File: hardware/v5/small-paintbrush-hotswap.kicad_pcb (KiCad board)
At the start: 2 copper layers, 97 x 50 mm, 21 parts, among them J1 Conn_01x02, J2 Conn_01x04, J3 Conn_01x04, SW1 SW_SPDT, SW2 SW_SPDT, U1 ProMicro, U2 ProMicro

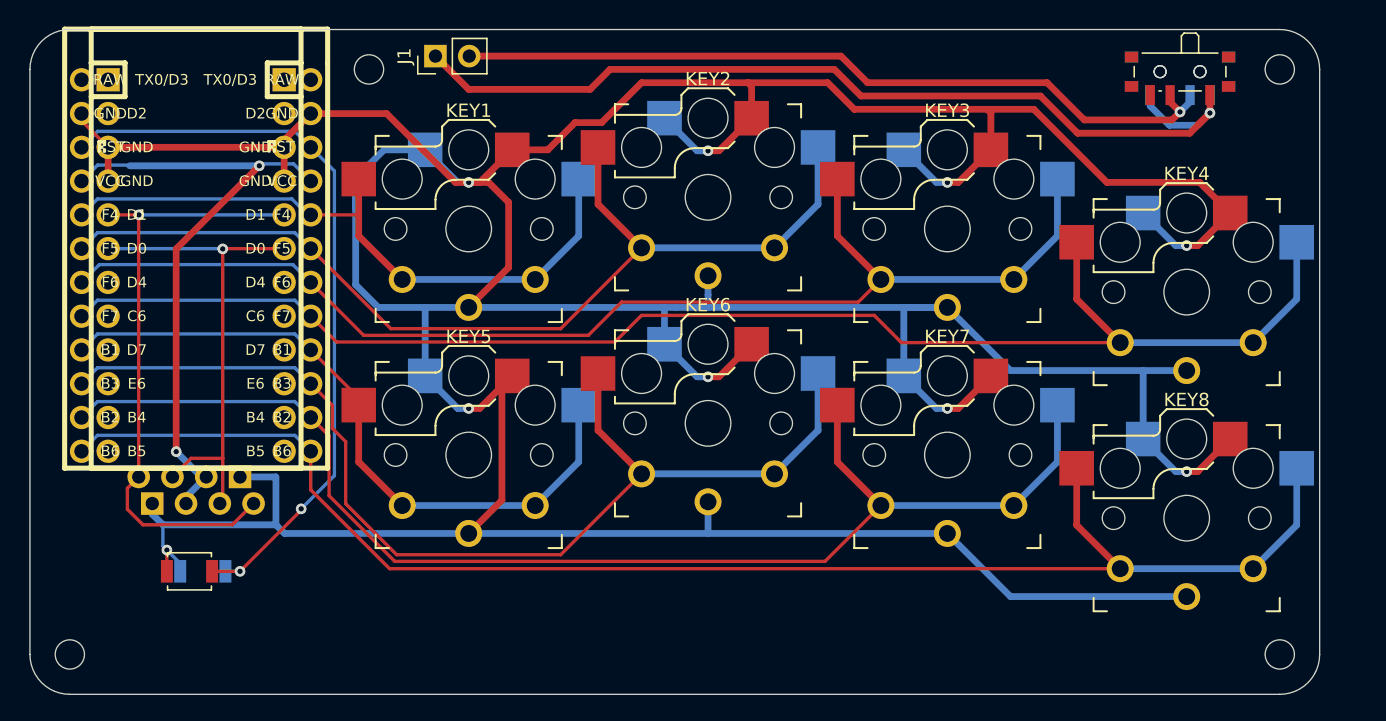
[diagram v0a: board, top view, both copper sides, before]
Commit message: v5 of the paintbrush with choc and mx hot swap switches (pcb size changed)
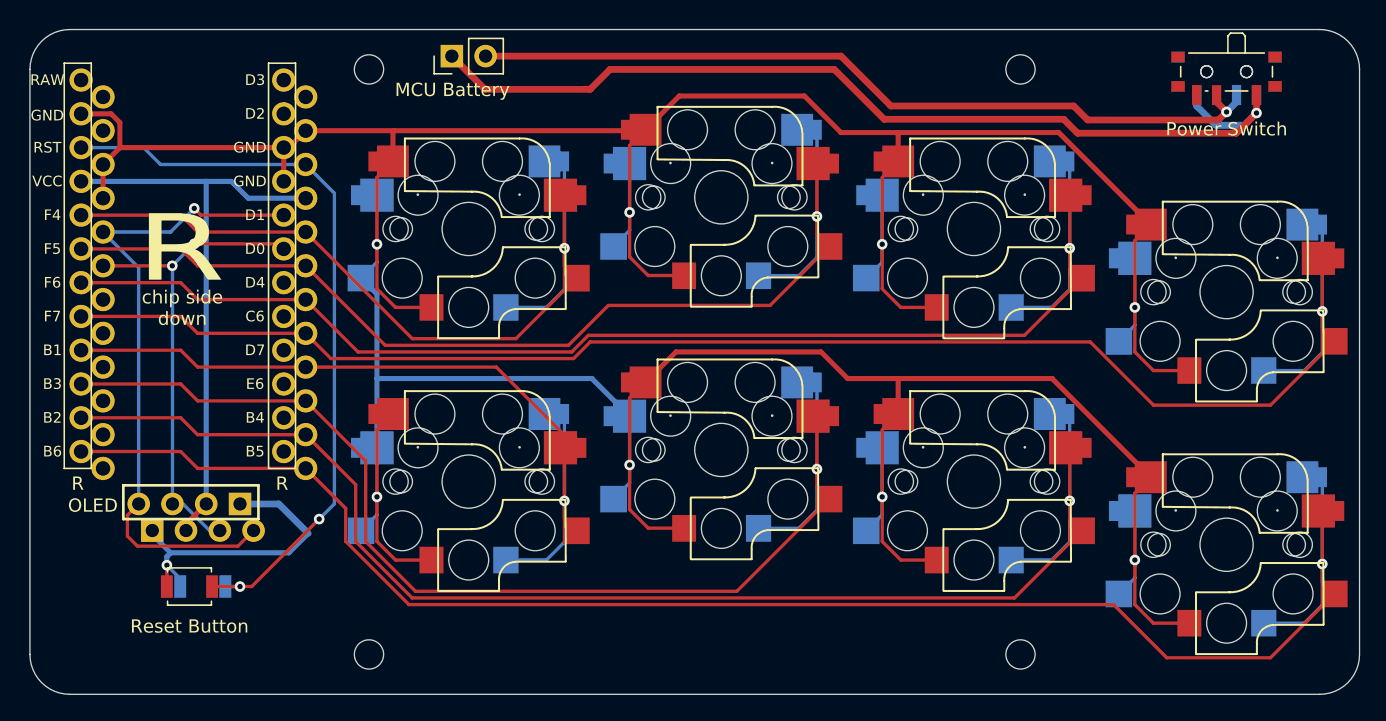
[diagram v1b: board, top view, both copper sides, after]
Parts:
- removed the REF** at (166.9, 65.6)
- removed the REF** at (75.9, 65.6)
- removed the REF** at (166.9, 21.6)
- added REF**: MountingHole_2.2mm_M2, MountingHole:MountingHole_2.2mm_M2, F.Cu at (147.4, 65.6)
- added REF**: MountingHole_2.2mm_M2, MountingHole:MountingHole_2.2mm_M2, F.Cu at (98.4, 65.6)
- added REF**: MountingHole_2.2mm_M2, MountingHole:MountingHole_2.2mm_M2, F.Cu at (147.4, 21.6)
- KEY1, KEY2, KEY3, KEY4, KEY5, KEY6, KEY7, KEY8: footprint keyswitches:Kailh_socket_PG1350_optional_reversible -> keyswitches:MX_Choc_Hotswap
- U1, U2: footprint Keebio-Parts:ArduinoProMicro -> small-paintbrush:promicro
- moved KEY8 3.61 mm to (162.9, 57.3)
- moved SW1 3.50 mm to (162.9, 22.1)
- moved SW2 3.50 mm to (162.9, 22.1)
- moved KEY4 3.00 mm to (162.9, 38.3)
- moved KEY7 2.83 mm to (143.9, 52.6)
- moved KEY6 2.24 mm to (124.9, 50.2)
- moved J2 2.03 mm to (78.9, 55.9)
- moved J3 2.03 mm to (91.9, 57.9)
- moved KEY3 2.00 mm to (143.9, 33.6)
- moved KEY5 2.00 mm to (105.9, 52.6)
- moved U2 1.25 mm to (84.4, 35.1)
- moved J1 1.23 mm to (104.6, 20.6)
- moved PUSH1 1.14 mm to (85.9, 60.5)
- moved PUSH2 1.14 mm to (84.9, 60.5)
- moved KEY2 1.00 mm to (124.9, 31.2)
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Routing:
- net GND: track 402.6 -> 374.5 mm
- net R2C4: track 112.4 -> 125.5 mm, vias 0 -> 1
- net R1C1: track 51.2 -> 64.3 mm, vias 0 -> 1
- net R1C4: track 109.8 -> 122.3 mm, vias 0 -> 1
- net R2C1: track 51.7 -> 61.2 mm, vias 0 -> 1
- net R2C3: track 97.8 -> 106.8 mm, vias 0 -> 1
- net R1C3: track 92.4 -> 101.1 mm, vias 0 -> 1
- net R2C2: track 82.5 -> 90.5 mm, vias 0 -> 1
- net R1C2: track 75.9 -> 83.7 mm, vias 0 -> 1
- net VCC: track 48.1 -> 44.3 mm, vias 2 -> 0
- net SDA: track 46.4 -> 49.2 mm
- net Net-(J1-Pad2): track 58.9 -> 61.1 mm
- net Net-(J1-Pad1): track 71.5 -> 73.7 mm
- net SCL: track 36.9 -> 36.8 mm, vias 1 -> 2
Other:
- board size 97 x 50 mm -> 100 x 50 mm
- board text added: "L"
- board text added: "MCU Battery"
- board text added: "OLED"
- board text added: "Power Switch"
- board text added: "R"
- board text added: "Reset Button"
- board text added: "chip side down"

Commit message: fix missing trace and gerbers for v5
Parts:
- removed the REF** at (147.4, 65.6)
- removed the REF** at (98.4, 65.6)
- removed the REF** at (147.4, 21.6)
- removed the REF** at (98.4, 21.6)
- added H1: MountingHole, small-paintbrush:mounting-holes, F.Cu at (122.9, 43.6)
- added REF**: MountingHole_2.1mm, MountingHole:MountingHole_2.1mm, F.Cu at (98.4, 65.6)
- added REF**: MountingHole_2.1mm, MountingHole:MountingHole_2.1mm, F.Cu at (147.4, 65.6)
- added REF**: MountingHole_2.1mm, MountingHole:MountingHole_2.1mm, F.Cu at (147.4, 21.6)
- added REF**: MountingHole_2.1mm, MountingHole:MountingHole_2.1mm, F.Cu at (98.4, 21.6)
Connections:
- SW1 pad 3: Net-(SW1-Pad3) -> (no net)
- SW2 pad 3: Net-(SW2-Pad3) -> (no net)
- U1 pad 1: Net-(U1-Pad1) -> (no net)
- U1 pad 10: Net-(U1-Pad10) -> (no net)
- U1 pad 11: Net-(U1-Pad11) -> (no net)
- U1 pad 12: Net-(U1-Pad12) -> (no net)
- U1 pad 2: Net-(U1-Pad2) -> (no net)
- U1 pad 24: Net-(U1-Pad24) -> (no net)
- U1 pad 7: Net-(U1-Pad7) -> (no net)
- U1 pad 8: Net-(U1-Pad8) -> (no net)
- U1 pad 9: Net-(U1-Pad9) -> (no net)
- U2 pad 1: Net-(U2-Pad1) -> (no net)
- U2 pad 10: Net-(U2-Pad10) -> (no net)
- U2 pad 11: Net-(U2-Pad11) -> (no net)
- U2 pad 12: Net-(U2-Pad12) -> (no net)
- U2 pad 2: Net-(U2-Pad2) -> (no net)
- U2 pad 24: Net-(U2-Pad24) -> (no net)
- U2 pad 7: Net-(U2-Pad7) -> (no net)
- U2 pad 8: Net-(U2-Pad8) -> (no net)
- U2 pad 9: Net-(U2-Pad9) -> (no net)
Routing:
- net GND: track 374.5 -> 378.5 mm
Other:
- outline, holes or cut-outs redrawn
